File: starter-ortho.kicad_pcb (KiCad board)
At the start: 2 copper layers, 272.3 x 82.6 mm, 98 parts, among them SW1 SW_Push, U1 ProMicro

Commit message: created splitish v2
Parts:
- added G***: LOGO, silkscreen:reid_face, B.Cu at (150.0, 73.0)
- D1, D10, D11, D12, D13, D14, D15, D16, D17, D18, D19, D2, D20, D21, D22, D23, D24, D25, D26, D27, D28, D29, D3, D30, D31, D32, D33, D34, D35, D36, D37, D38, D39, D4, D40, D41, D42, D43, D44, D45, D46, D47, D48, D5, D6, D7, D8, D9: moved to F.Cu
- moved D41 17.7 mm to (244.5, 25.4)
- moved D42 17.7 mm to (244.5, 44.5)
- moved D43 17.7 mm to (244.5, 63.5)
- moved D29 17.6 mm to (187.3, 25.4)
- moved D33 17.6 mm to (206.4, 25.4)
- moved D37 17.6 mm to (225.4, 25.4)
- moved D48 17.6 mm to (263.5, 82.5)
- moved D25 17.5 mm to (168.3, 25.4)
- moved D27 17.5 mm to (168.3, 63.5)
- moved D30 17.5 mm to (187.3, 44.5)
- moved D31 17.5 mm to (187.3, 63.5)
- moved D34 17.5 mm to (206.4, 44.5)
- moved D35 17.5 mm to (206.4, 63.5)
- moved D38 17.5 mm to (225.4, 44.5)
- moved D39 17.5 mm to (225.4, 63.5)
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- renumbered SW1 to RESET
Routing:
- net GND: track 50.5 -> 8.73 mm, vias 0 -> 1
- net ROW0: track 272.7 -> 246.8 mm
- net COL0: track 192.9 -> 218.5 mm, vias 0 -> 1
- net ROW2: track 281.4 -> 259.4 mm
- net ROW3: track 294.3 -> 275.9 mm
- net ROW1: track 254.0 -> 236.5 mm
- net COL11: track 184.4 -> 194.2 mm, vias 0 -> 1
- net COL10: track 165.4 -> 172.1 mm, vias 0 -> 1
- net COL1: track 174.1 -> 179.0 mm, vias 0 -> 1
- net COL5: track 94.4 -> 91.7 mm, vias 0 -> 1
- net COL4: track 113.0 -> 110.8 mm, vias 0 -> 1
- net COL3: track 131.6 -> 129.4 mm, vias 0 -> 1
- net COL2: track 151.5 -> 149.8 mm, vias 0 -> 1
- net Net-(D42-Pad2): track 13.0 -> 11.7 mm
- net Net-(D17-Pad2): track 12.5 -> 11.7 mm
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- added copper zone on B.Cu, net GND
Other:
- board size 272.3 x 82.6 mm -> 271.5 x 81 mm
- board text added: "by Reid"
- board text added: "splitish"
- board text added: "v2"

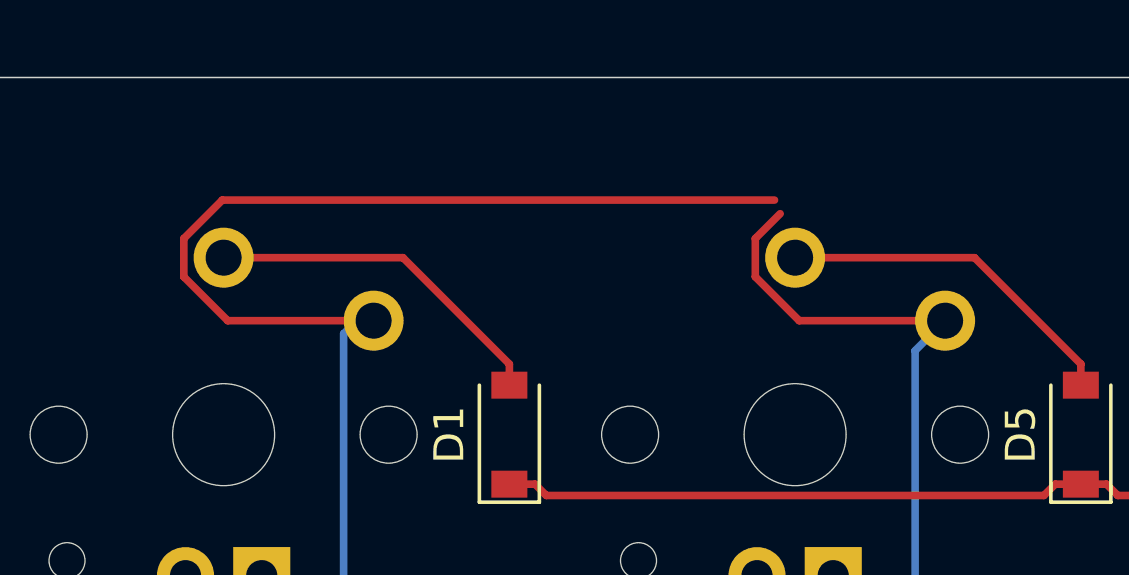
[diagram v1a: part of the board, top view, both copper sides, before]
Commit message: deleted unused traces and remade gerbers
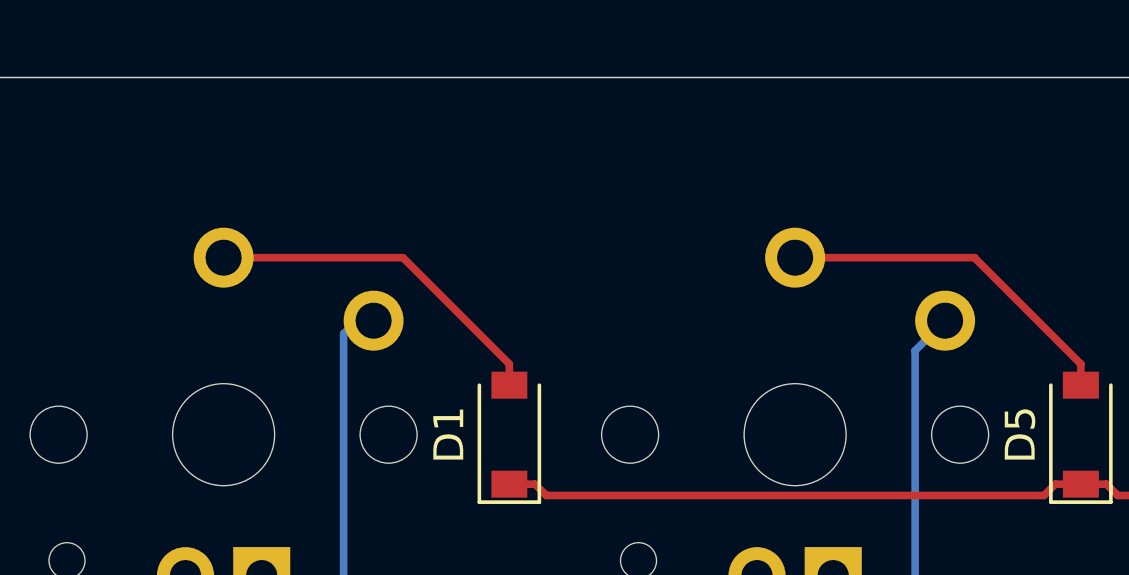
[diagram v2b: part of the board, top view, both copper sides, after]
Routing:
- net COL0: track 218.5 -> 190.1 mm
- net COL1: track 179.0 -> 169.6 mm
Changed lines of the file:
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@@
     (thickness 1.6)
     (drawings 12)
-    (tracks 606)
+    (tracks 597)
     (zones 0)
     (modules 99)
@@
     (add_net GND)
   )
+  (module Kailh_Choc:KailhChoc-1U (layer F.Cu)
+    (at 44.45 25.4)
+    (fp_text reference MX5 (at 0 3.175) (layer Dwgs.User)
+      (effects (font (size 1 1) (thickness 0.15)))
+    )
+    (fp_text value MX-NoLED (at 0 -7.9375) (layer Dwgs.User)
+      (effects (font (size 1 1) (thickness 0.15)))
+    )
+    (fp_line (start -9.525 9.525) (end -9.525 -9.525) (layer Dwgs.User) (width 0.15))
+    (fp_line (start 9.525 9.525) (end -9.525 9.525) (layer Dwgs.User) (width 0.15))
+    (fp_line (start 9.525 -9.525) (end 9.525 9.525) (layer Dwgs.User) (width 0.15))
+    (fp_line (start -9.525 -9.525) (end 9.525 -9.525) (layer Dwgs.User) (width 0.15))
+    (fp_line (start -7 -7) (end -7 -5) (layer Dwgs.User) (width 0.15))
+    (fp_line (start -5 -7) (end -7 -7) (layer Dwgs.User) (width 0.15))
+    (fp_line (start -7 7) (end -5 7) (layer Dwgs.User) (width 0.15))
+    (fp_line (start -7 5) (end -7 7) (layer Dwgs.User) (width 0.15))
+    (fp_line (start 7 7) (end 7 5) (layer Dwgs.User) (width 0.15))
+    (fp_line (start 5 7) (end 7 7) (layer Dwgs.User) (width 0.15))
+    (fp_line (start 7 -7) (end 7 -5) (layer Dwgs.User) (width 0.15))
+    (fp_line (start 5 -7) (end 7 -7) (layer Dwgs.User) (width 0.15))
+    (pad 4 thru_hole rect (at 1.27 4.7) (size 1.905 1.905) (drill 1.04) (layers *.Cu B.Mask))
+    (pad 3 thru_hole circle (at -1.27 4.7) (size 1.905 1.905) (drill 1.04) (layers *.Cu B.Mask))
+    (pad "" np_thru_hole circle (at -5.22 4.2) (size 1.2 1.2) (drill 1.2) (layers *.Cu *.Mask))
+    (pad "" np_thru_hole circle (at 5.5 0 48.1) (size 1.9 1.9) (drill 1.9) (layers *.Cu *.Mask))
+    (pad "" np_thru_hole circle (at -5.5 0 48.1) (size 1.9 1.9) (drill 1.9) (layers *.Cu *.Mask))
+    (pad 1 thru_hole circle (at 5 -3.8) (size 2 2) (drill 1.2) (layers *.Cu B.Mask)
+      (net 54 COL1))
+    (pad "" np_thru_hole circle (at 0 0) (size 3.4 3.4) (drill 3.4) (layers *.Cu *.Mask))
+    (pad 2 thru_hole circle (at 0 -5.9) (size 2 2) (drill 1.2) (layers *.Cu B.Mask)
+      (net 9 "Net-(D5-Pad2)"))
+  )
   (module silkscreen:reid_face (layer B.Cu)
     (at 150.01875 73.025 180)
@@
   )
   (module Kailh_Choc:KailhChoc-1U (layer F.Cu)
-    (at 44.45 25.4)
-    (fp_text reference MX5 (at 0 3.175) (layer Dwgs.User)
-      (effects (font (size 1 1) (thickness 0.15)))
-    )
-    (fp_text value MX-NoLED (at 0 -7.9375) (layer Dwgs.User)
-      (effects (font (size 1 1) (thickness 0.15)))
-    )
-    (fp_line (start -9.525 9.525) (end -9.525 -9.525) (layer Dwgs.User) (width 0.15))
-    (fp_line (start 9.525 9.525) (end -9.525 9.525) (layer Dwgs.User) (width 0.15))
-    (fp_line (start 9.525 -9.525) (end 9.525 9.525) (layer Dwgs.User) (width 0.15))
-    (fp_line (start -9.525 -9.525) (end 9.525 -9.525) (layer Dwgs.User) (width 0.15))
-    (fp_line (start -7 -7) (end -7 -5) (layer Dwgs.User) (width 0.15))
-    (fp_line (start -5 -7) (end -7 -7) (layer Dwgs.User) (width 0.15))
-    (fp_line (start -7 7) (end -5 7) (layer Dwgs.User) (width 0.15))
-    (fp_line (start -7 5) (end -7 7) (layer Dwgs.User) (width 0.15))
-    (fp_line (start 7 7) (end 7 5) (layer Dwgs.User) (width 0.15))
-    (fp_line (start 5 7) (end 7 7) (layer Dwgs.User) (width 0.15))
-    (fp_line (start 7 -7) (end 7 -5) (layer Dwgs.User) (width 0.15))
-    (fp_line (start 5 -7) (end 7 -7) (layer Dwgs.User) (width 0.15))
-    (pad 4 thru_hole rect (at 1.27 4.7) (size 1.905 1.905) (drill 1.04) (layers *.Cu B.Mask))
-    (pad 3 thru_hole circle (at -1.27 4.7) (size 1.905 1.905) (drill 1.04) (layers *.Cu B.Mask))
-    (pad "" np_thru_hole circle (at -5.22 4.2) (size 1.2 1.2) (drill 1.2) (layers *.Cu *.Mask))
-    (pad "" np_thru_hole circle (at 5.5 0 48.1) (size 1.9 1.9) (drill 1.9) (layers *.Cu *.Mask))
-    (pad "" np_thru_hole circle (at -5.5 0 48.1) (size 1.9 1.9) (drill 1.9) (layers *.Cu *.Mask))
-    (pad 1 thru_hole circle (at 5 -3.8) (size 2 2) (drill 1.2) (layers *.Cu B.Mask)
-      (net 54 COL1))
-    (pad "" np_thru_hole circle (at 0 0) (size 3.4 3.4) (drill 3.4) (layers *.Cu *.Mask))
-    (pad 2 thru_hole circle (at 0 -5.9) (size 2 2) (drill 1.2) (layers *.Cu B.Mask)
-      (net 9 "Net-(D5-Pad2)"))
-  )
-  (module Kailh_Choc:KailhChoc-1U (layer F.Cu)
     (at 25.4 82.55)
     (fp_text reference MX4 (at 0 3.175) (layer Dwgs.User)
@@
   (segment (start 30.4 21.6) (end 29.835 21.6) (width 0.254) (layer B.Cu) (net 53))
   (segment (start 29.835 21.6) (end 29.400001 22.034999) (width 0.254) (layer B.Cu) (net 53))
-  (segment (start 24.072999 18.863039) (end 25.356048 17.57999) (width 0.254) (layer F.Cu) (net 53))
-  (segment (start 24.072999 20.136961) (end 24.072999 18.863039) (width 0.254) (layer F.Cu) (net 53))
-  (segment (start 30.4 21.6) (end 25.536038 21.6) (width 0.254) (layer F.Cu) (net 53))
-  (segment (start 25.536038 21.6) (end 24.072999 20.136961) (width 0.254) (layer F.Cu) (net 53))
-  (segment (start 25.356048 17.57999) (end 43.763981 17.57999) (width 0.254) (layer F.Cu) (net 53))
   (via (at 129.667 31.702985) (size 0.8) (drill 0.4) (layers F.Cu B.Cu) (net 53))
   (segment (start 30.4 40.65) (end 25.536038 40.65) (width 0.254) (layer F.Cu) (net 53))
@@
   (segment (start 48.450001 60.699999) (end 48.450001 77.750001) (width 0.254) (layer B.Cu) (net 54))
   (segment (start 49.45 59.7) (end 48.450001 60.699999) (width 0.254) (layer B.Cu) (net 54))
-  (segment (start 43.122999 18.863039) (end 43.952038 18.034) (width 0.254) (layer F.Cu) (net 54))
-  (segment (start 43.122999 20.136961) (end 43.122999 18.863039) (width 0.254) (layer F.Cu) (net 54))
-  (segment (start 49.45 21.6) (end 44.586038 21.6) (width 0.254) (layer F.Cu) (net 54))
-  (segment (start 44.586038 21.6) (end 43.122999 20.136961) (width 0.254) (layer F.Cu) (net 54))
   (via (at 129.667 32.702988) (size 0.8) (drill 0.4) (layers F.Cu B.Cu) (net 54))
   (segment (start 44.586038 40.65) (end 43.122999 39.186961) (width 0.254) (layer F.Cu) (net 54))
